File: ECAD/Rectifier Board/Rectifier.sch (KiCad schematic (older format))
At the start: 22 parts

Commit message: resonant
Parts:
- removed C? (x3): 1uF, symbol Device:C
- removed R?: 11K, symbol Device:R
- removed R?: 1K, symbol Device:R
- removed U?: LM317_TO-220, Package_TO_SOT_THT:TO-220-3_Vertical, symbol Regulator_Linear:LM317_TO-220
- added U?: NCP1380C, Package_SO:SOIC-8_3.9x4.9mm_P1.27mm, symbol Regulator_Controller:NCP1380C
- J?: value 25VAC -> 120VAC
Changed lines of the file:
@@
 P 2150 3000
 F 0 "J?" H 2068 2675 50  0000 C CNN
-F 1 "25VAC" H 2068 2766 50  0000 C CNN
+F 1 "120VAC" H 2068 2766 50  0000 C CNN
 F 2 "" H 2150 3000 50  0001 C CNN
 F 3 "~" H 2150 3000 50  0001 C CNN
@@
 $EndComp
 $Comp
-L Regulator_Linear:LM317_TO-220 U?
-U 1 1 6205D4E8
-P 5050 2900
-F 0 "U?" H 5050 3142 50  0000 C CNN
-F 1 "LM317_TO-220" H 5050 3051 50  0000 C CNN
-F 2 "Package_TO_SOT_THT:TO-220-3_Vertical" H 5050 3150 50  0001 C CIN
-F 3 "http://www.ti.com/lit/ds/symlink/lm317.pdf" H 5050 2900 50  0001 C CNN
-	1    5050 2900
-	1    0    0    -1
-$EndComp
-$Comp
-L Device:R R?
-U 1 1 6205E083
-P 5050 3350
-F 0 "R?" H 5100 3350 50  0000 L CNN
-F 1 "11K" V 5050 3350 50  0000 C CNN
-F 2 "" V 4980 3350 50  0001 C CNN
-F 3 "~" H 5050 3350 50  0001 C CNN
-	1    5050 3350
-	1    0    0    -1
-$EndComp
-$Comp
-L Device:R R?
-U 1 1 6205F378
-P 5500 3050
-F 0 "R?" H 5550 3050 50  0000 L CNN
-F 1 "1K" V 5500 3050 50  0000 C CNN
-F 2 "" V 5430 3050 50  0001 C CNN
-F 3 "~" H 5500 3050 50  0001 C CNN
-	1    5500 3050
-	1    0    0    -1
-$EndComp
-Wire Wire Line
-	5050 3200 5500 3200
-Connection ~ 5050 3200
-Wire Wire Line
-	5500 2900 5350 2900
-$Comp
-L Device:C C?
-U 1 1 6205FE8A
-P 5800 3050
-F 0 "C?" H 5915 3096 50  0000 L CNN
-F 1 "1uF" H 5915 3005 50  0000 L CNN
-F 2 "" H 5838 2900 50  0001 C CNN
-F 3 "~" H 5800 3050 50  0001 C CNN
-	1    5800 3050
-	1    0    0    -1
-$EndComp
-$Comp
-L Device:C C?
-U 1 1 620613FC
-P 5500 3350
-F 0 "C?" H 5615 3396 50  0000 L CNN
-F 1 "1uF" H 5615 3305 50  0000 L CNN
-F 2 "" H 5538 3200 50  0001 C CNN
-F 3 "~" H 5500 3350 50  0001 C CNN
-	1    5500 3350
-	1    0    0    -1
-$EndComp
-Connection ~ 5500 3200
-Wire Wire Line
-	5800 3500 5800 3200
-Wire Wire Line
-	5800 2900 5500 2900
-Connection ~ 5500 2900
-$Comp
-L Device:C C?
-U 1 1 620625CD
-P 4400 3050
-F 0 "C?" H 4515 3096 50  0000 L CNN
-F 1 "1uF" H 4515 3005 50  0000 L CNN
-F 2 "" H 4438 2900 50  0001 C CNN
-F 3 "~" H 4400 3050 50  0001 C CNN
-	1    4400 3050
-	1    0    0    -1
-$EndComp
-Wire Wire Line
-	4400 3500 4400 3200
-Wire Wire Line
-	4750 2900 4400 2900
-$Comp
 L Device:CP C?
 U 1 1 62063BAE
@@
 Wire Wire Line
 	3950 3500 3950 3150
-Wire Wire Line
-	3950 2150 4400 2150
 Connection ~ 3950 2150
-Wire Wire Line
-	3950 3500 4400 3500
 Connection ~ 3950 3500
-$Comp
-L power:+15V #PWR?
-U 1 1 6206D11A
-P 5800 2900
-F 0 "#PWR?" H 5800 2750 50  0001 C CNN
-F 1 "+15V" H 5815 3073 50  0000 C CNN
-F 2 "" H 5800 2900 50  0001 C CNN
-F 3 "" H 5800 2900 50  0001 C CNN
-	1    5800 2900
-	1    0    0    -1
-$EndComp
-Connection ~ 5800 2900
 $Comp
 L power:+15V #PWR?
@@
 	6650 3500 6750 3500
 Wire Wire Line
-	4400 2150 4400 2900
-Connection ~ 4400 2900
-Wire Wire Line
 	3950 2150 3950 2850
 Wire Wire Line
@@
 Wire Wire Line
 	8400 3500 7500 3500
-Connection ~ 4400 2150
-Connection ~ 4400 3500
-Connection ~ 5050 3500
-Connection ~ 5500 3500
-Connection ~ 5800 3500
-Wire Wire Line
-	5050 3500 5500 3500
-Wire Wire Line
-	5500 3500 5800 3500
-Wire Wire Line
-	4400 3500 5050 3500
-Wire Wire Line
-	5800 3500 6050 3500
 $Comp
 L Device:CP C?
@@
 $EndComp
 Wire Wire Line
-	4400 2150 6050 2150
-Wire Wire Line
 	6050 2300 6050 2150
 Connection ~ 6050 2150
@@
 Wire Wire Line
 	6050 3500 6250 3500
+Wire Wire Line
+	3950 3500 6050 3500
+Wire Wire Line
+	3950 2150 6050 2150
+$Comp
+L Regulator_Controller:NCP1380C U?
+U 1 1 6212BD3D
+P 6450 4750
+F 0 "U?" H 6450 5331 50  0000 C CNN
+F 1 "NCP1380C" H 6450 5240 50  0000 C CNN
+F 2 "Package_SO:SOIC-8_3.9x4.9mm_P1.27mm" H 6450 4750 50  0001 C CIN
+F 3 "https://www.onsemi.com/pub/Collateral/NCP1380-D.PDF" H 6450 4750 50  0001 C CNN
+	1    6450 4750
+	1    0    0    -1
+$EndComp
 $EndSCHEMATC

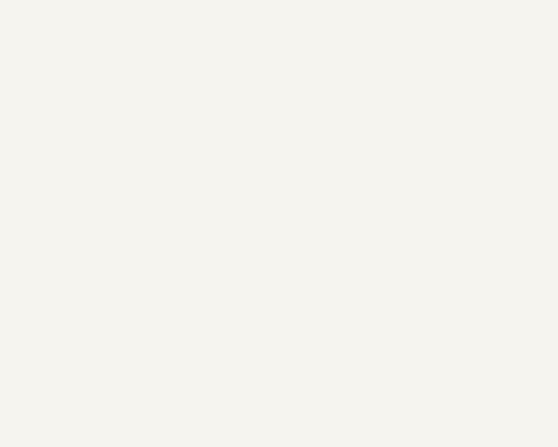
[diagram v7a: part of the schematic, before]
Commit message: route out larger planes
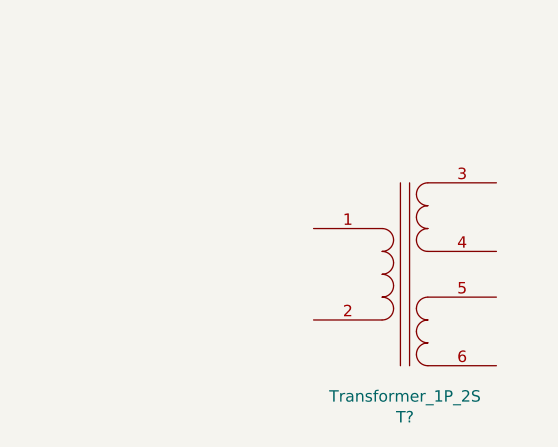
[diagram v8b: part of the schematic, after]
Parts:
- added T?: Transformer_1P_2S, symbol Device:Transformer_1P_2S
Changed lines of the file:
@@
+	1    0    0    -1
+$EndComp
+$Comp
+L Device:Transformer_1P_2S T?
+U 1 1 6213DB4F
+P 9150 5050
+F 0 "T?" H 9150 4425 50  0000 C CNN
+F 1 "Transformer_1P_2S" H 9150 4516 50  0000 C CNN
+F 2 "" H 9150 5050 50  0001 C CNN
+F 3 "~" H 9150 5050 50  0001 C CNN
+	1    9150 5050
 	1    0    0    -1
 $EndComp
